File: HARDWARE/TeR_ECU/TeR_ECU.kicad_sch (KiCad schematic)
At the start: 6 parts, among them U7 HDSP-A153

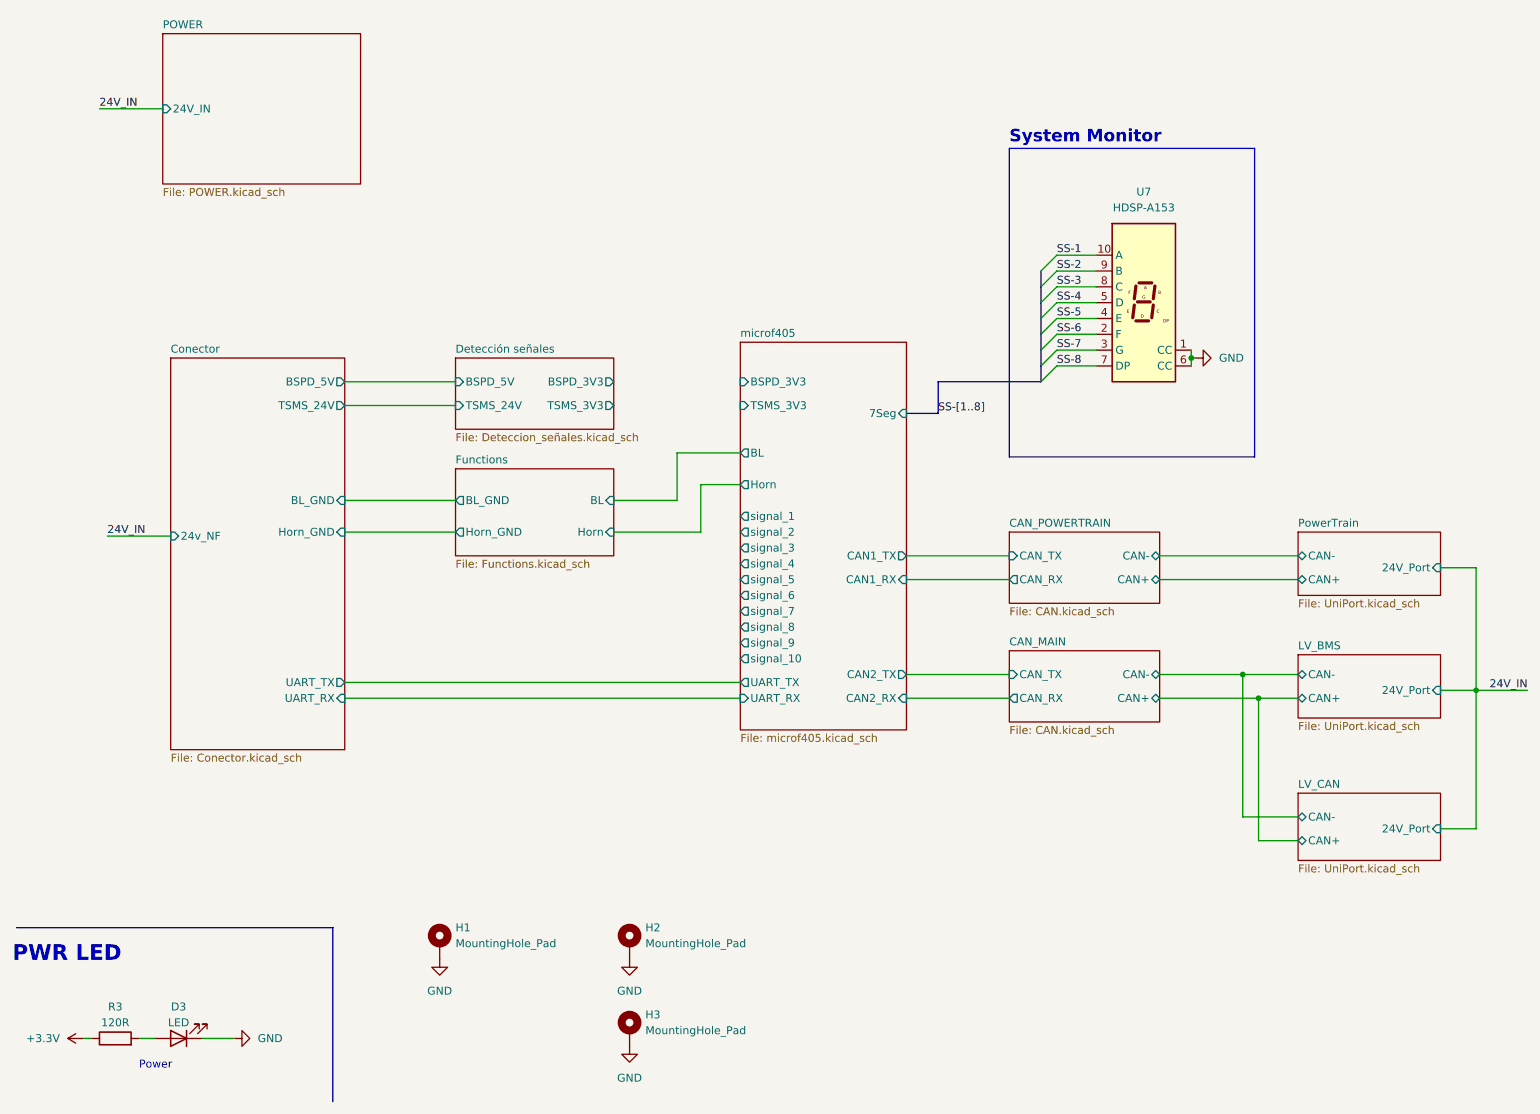
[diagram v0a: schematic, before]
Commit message: idea de esquema de safety y level shifter para señales de 24v
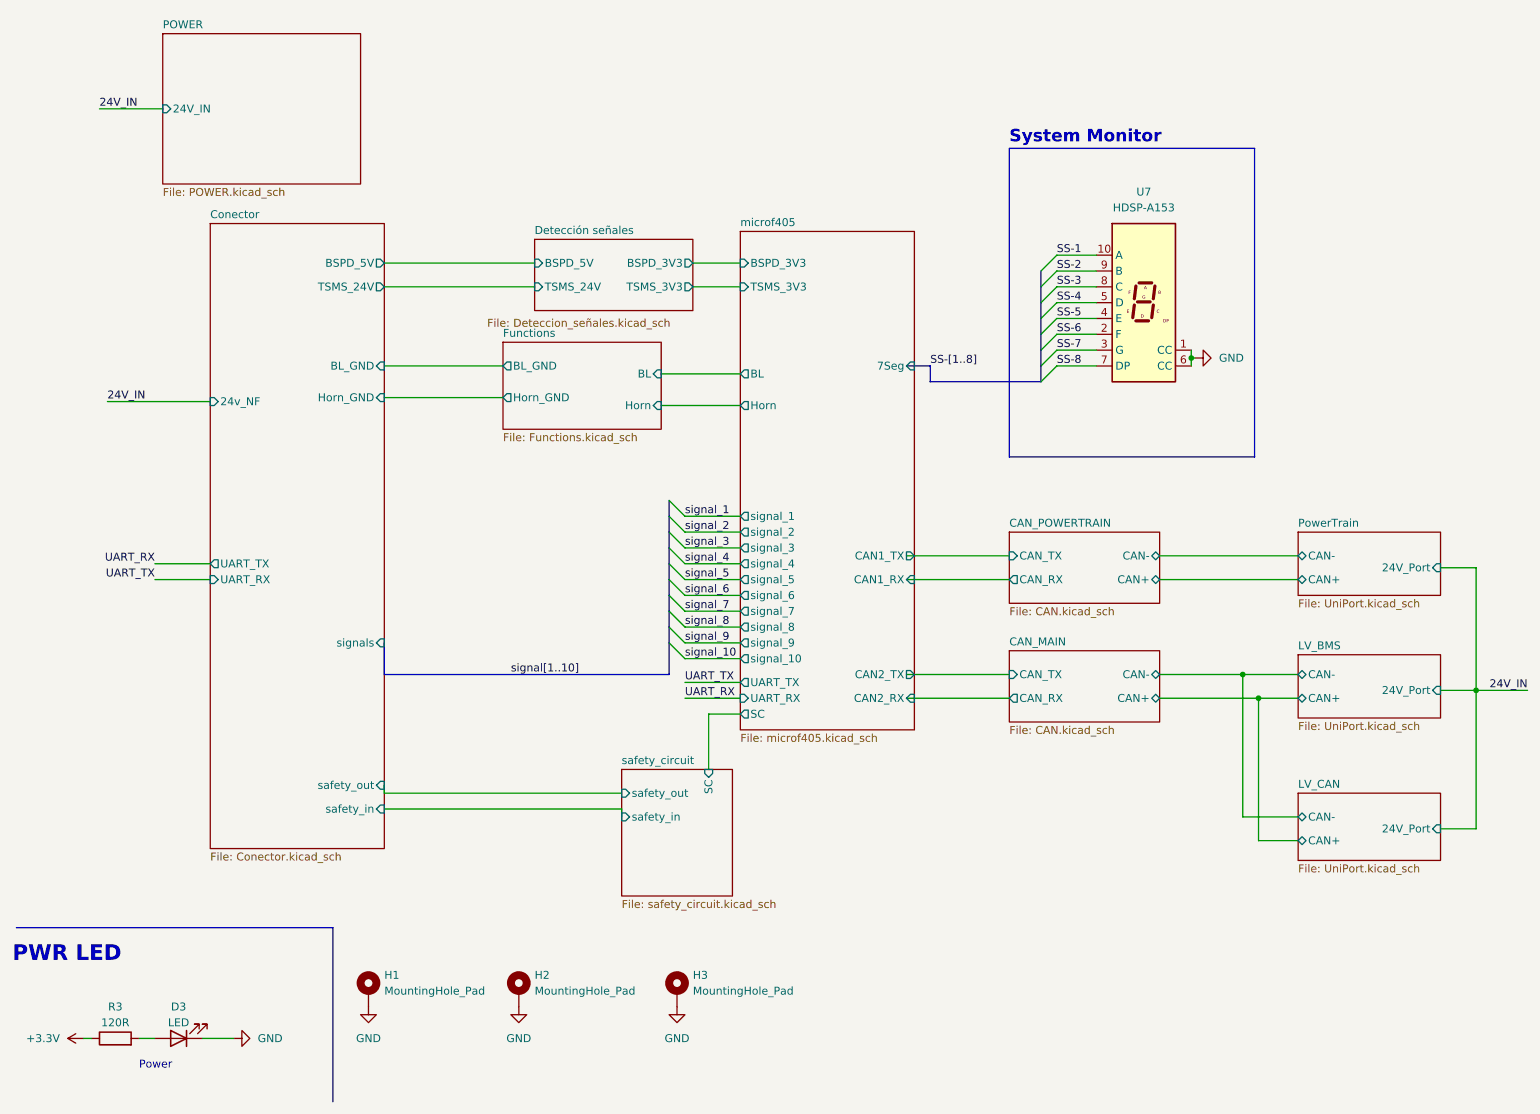
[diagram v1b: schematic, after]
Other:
- added sheet safety_circuit (safety_circuit.kicad_sch)
- sheet Conector ports: added safety_in, safety_out, signals; removed none
- sheet microf405 ports: added SC; removed none
- moved on the sheet: H1, H2, H3

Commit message: sd añadida, uniport redundante eliminado
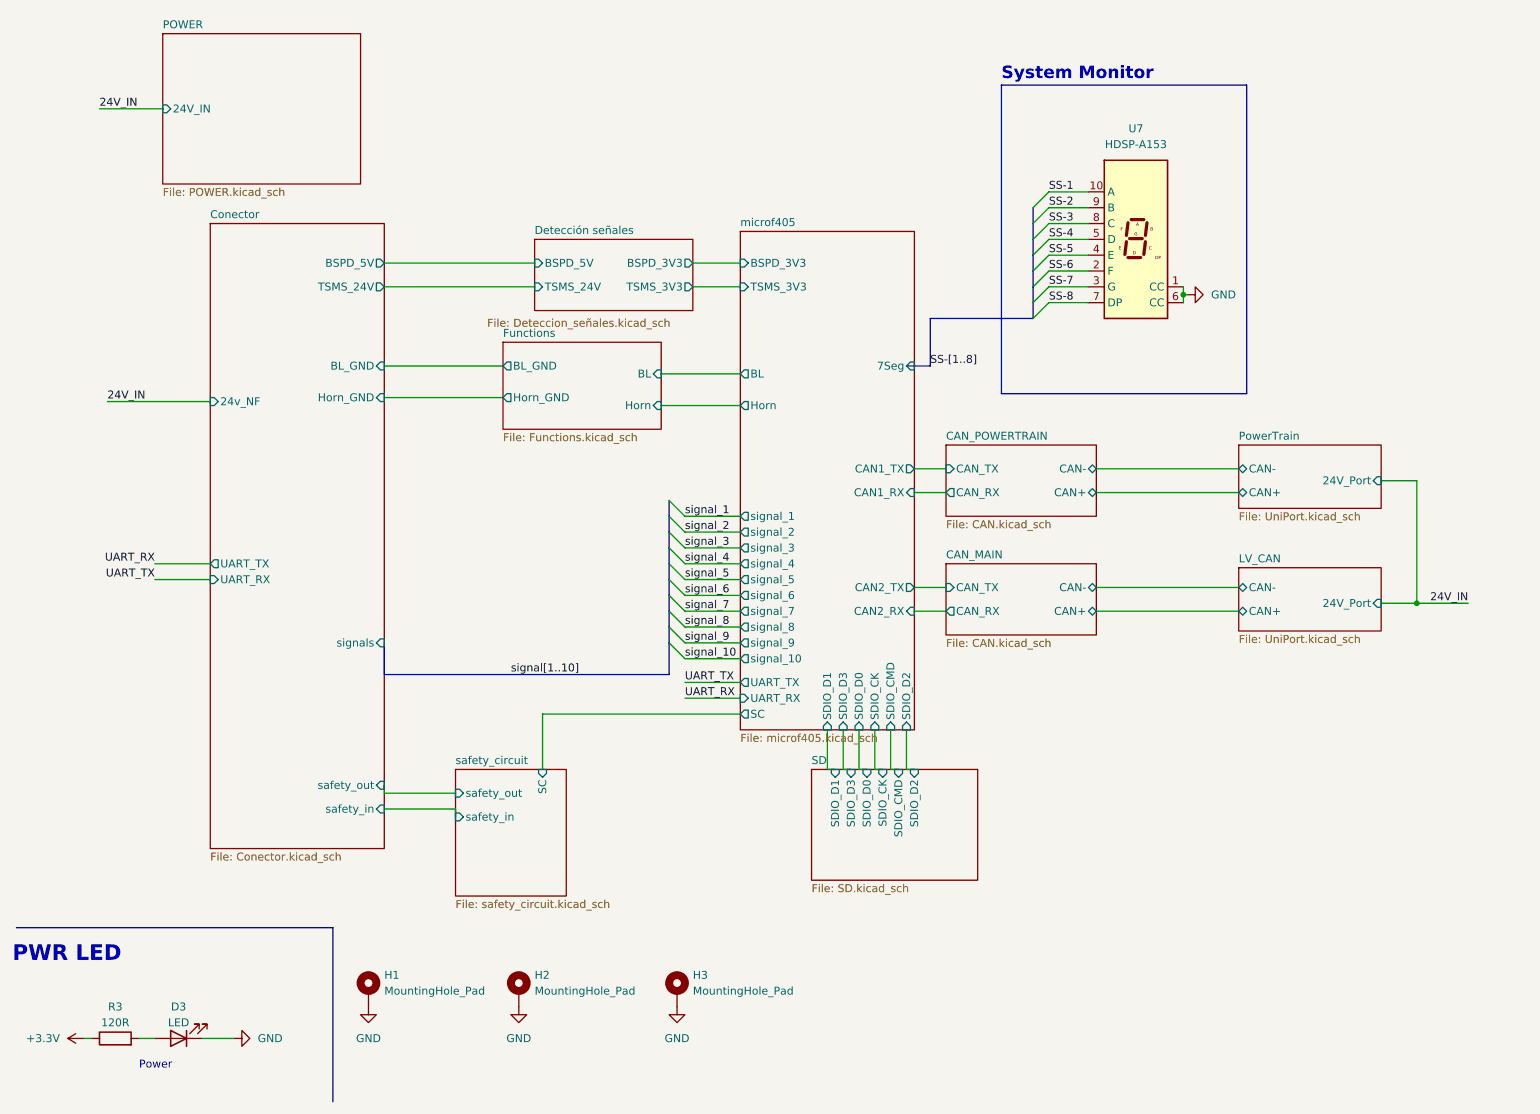
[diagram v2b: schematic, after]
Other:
- removed sheet LV_BMS
- added sheet SD (SD.kicad_sch)
- sheet microf405 ports: added SDIO_CK, SDIO_CMD, SDIO_D0, SDIO_D1, SDIO_D2, SDIO_D3; removed none
- moved on the sheet: U7

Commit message: usb-c, good debug conn, switch
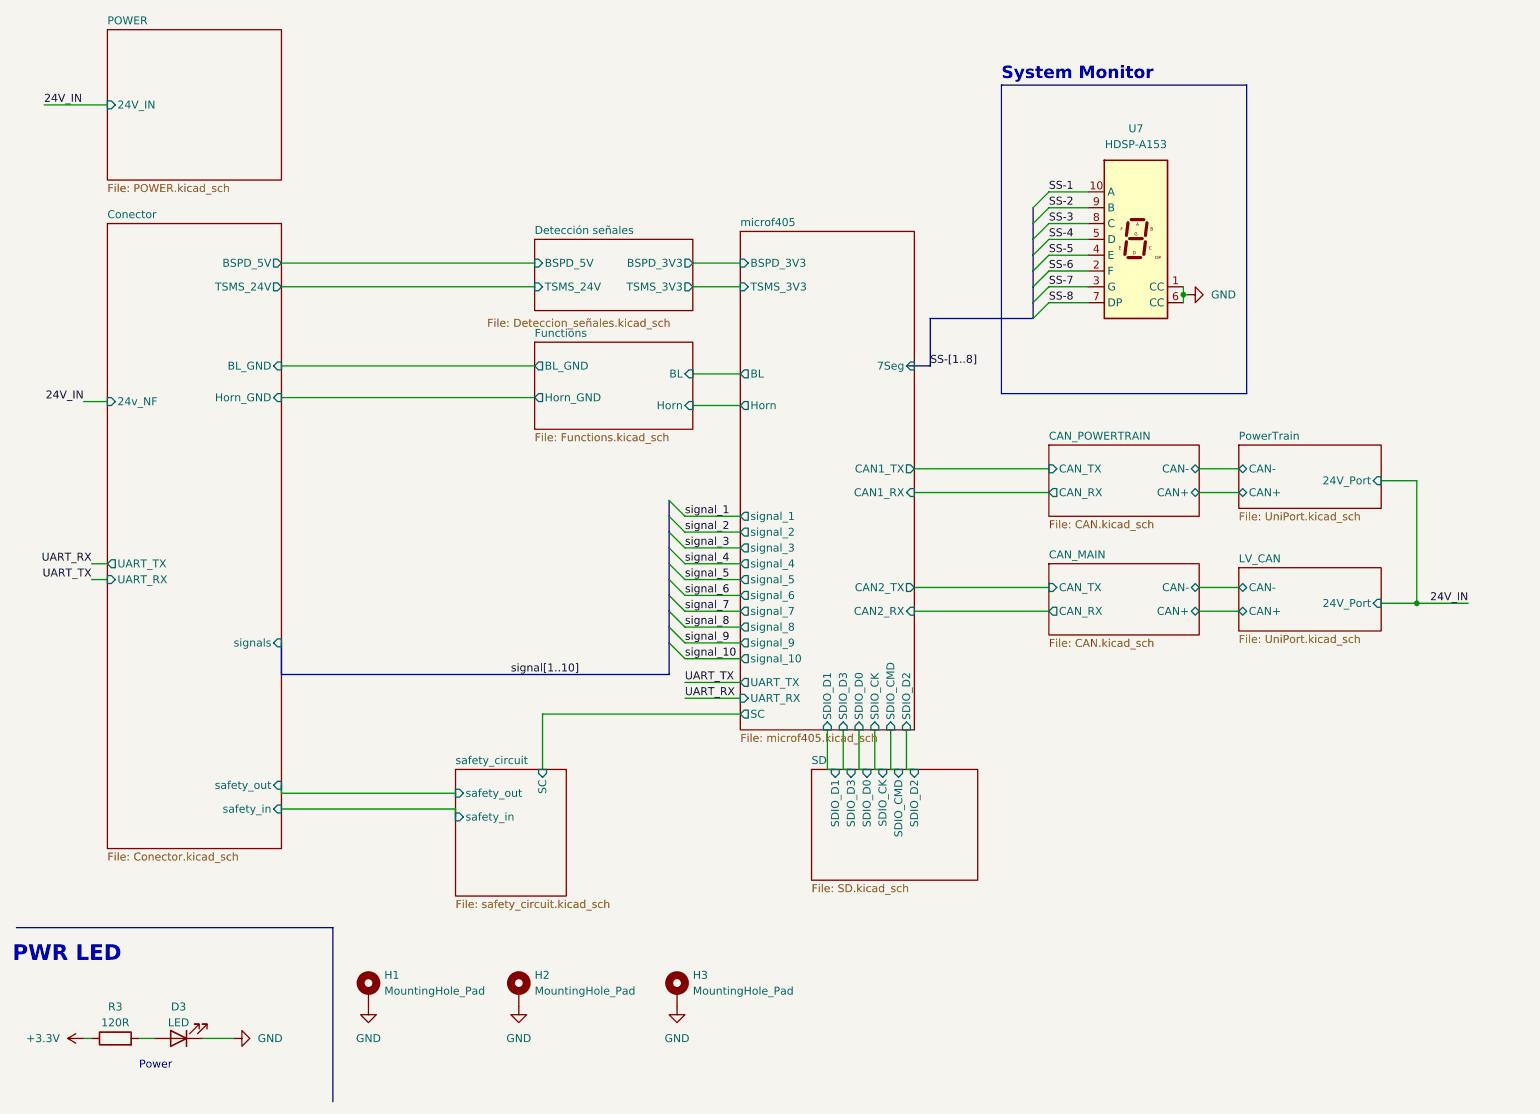
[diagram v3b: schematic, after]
